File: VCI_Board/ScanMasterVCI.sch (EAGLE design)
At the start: 43 parts, among them IC1 XMEGA16A4A, IC4 SN74AHCT1G04, IC5 SN74AHCT1G04, Q5 PZT3904, Q6 MMBT3904, Q7 MMBT4403, Q8 MMBT3904/SOT, U1 MAX13444EASA+, U2 LM339MA

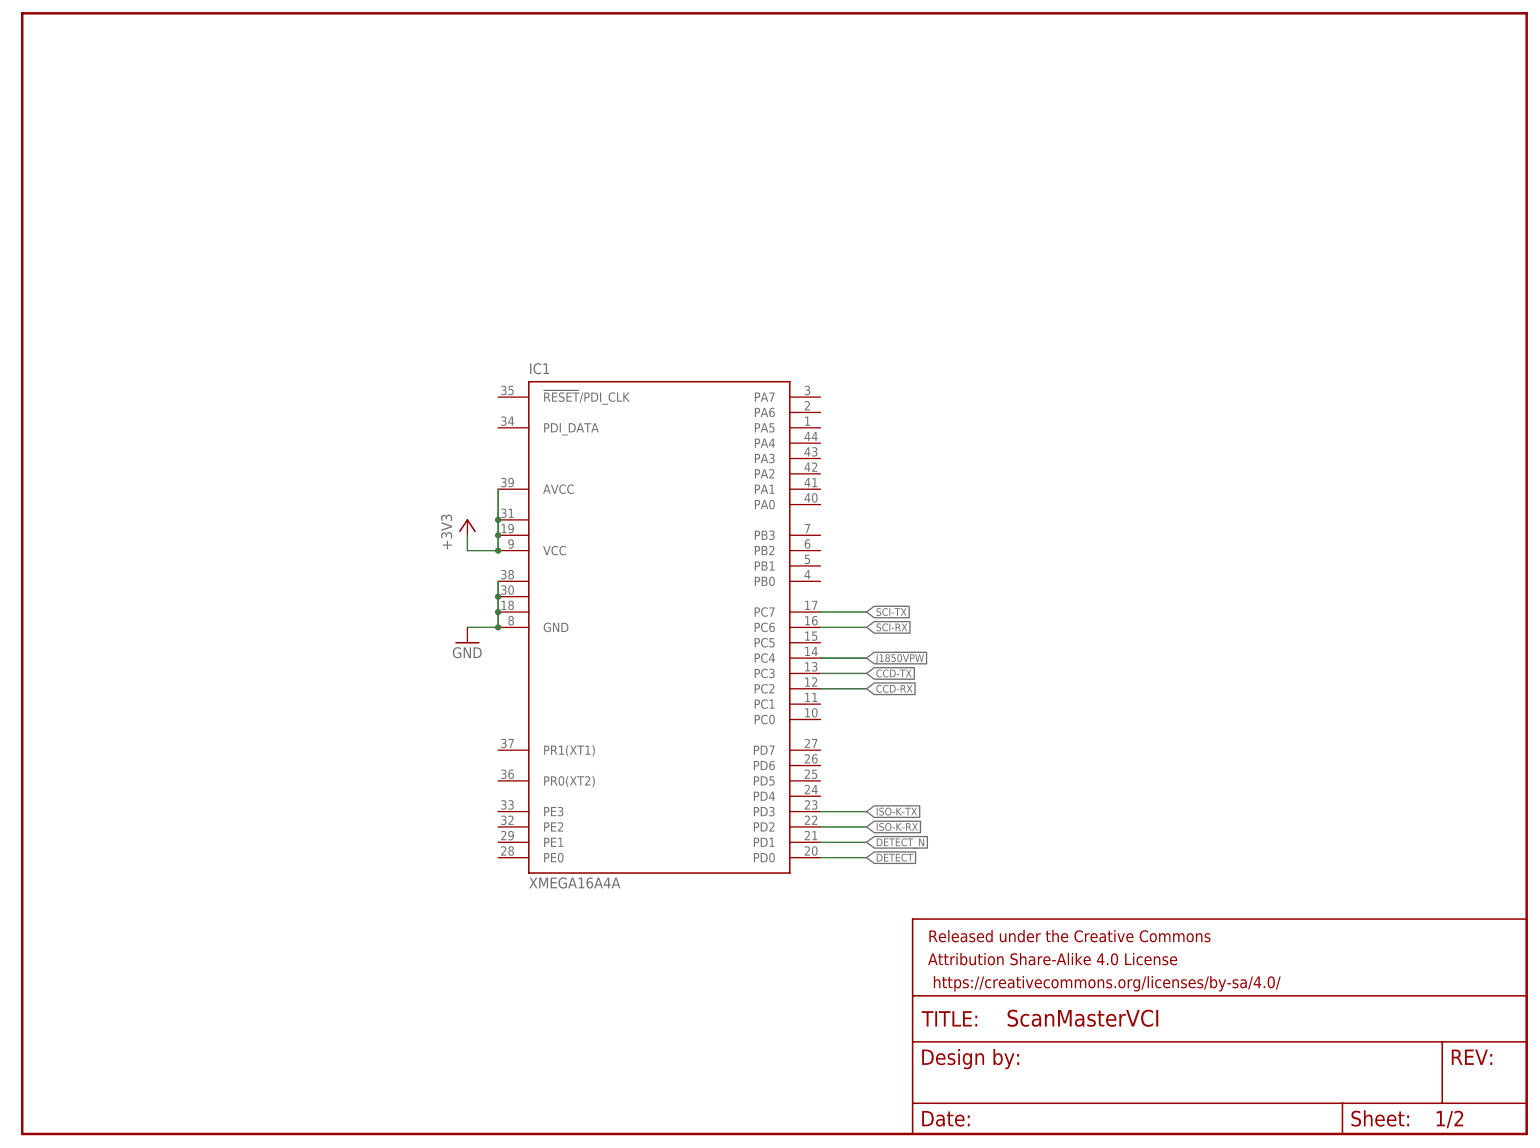
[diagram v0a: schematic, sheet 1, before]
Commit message: Begun redesigning CCD circuit. I originally based it off a J1708 circuit I found but realized that would not work.
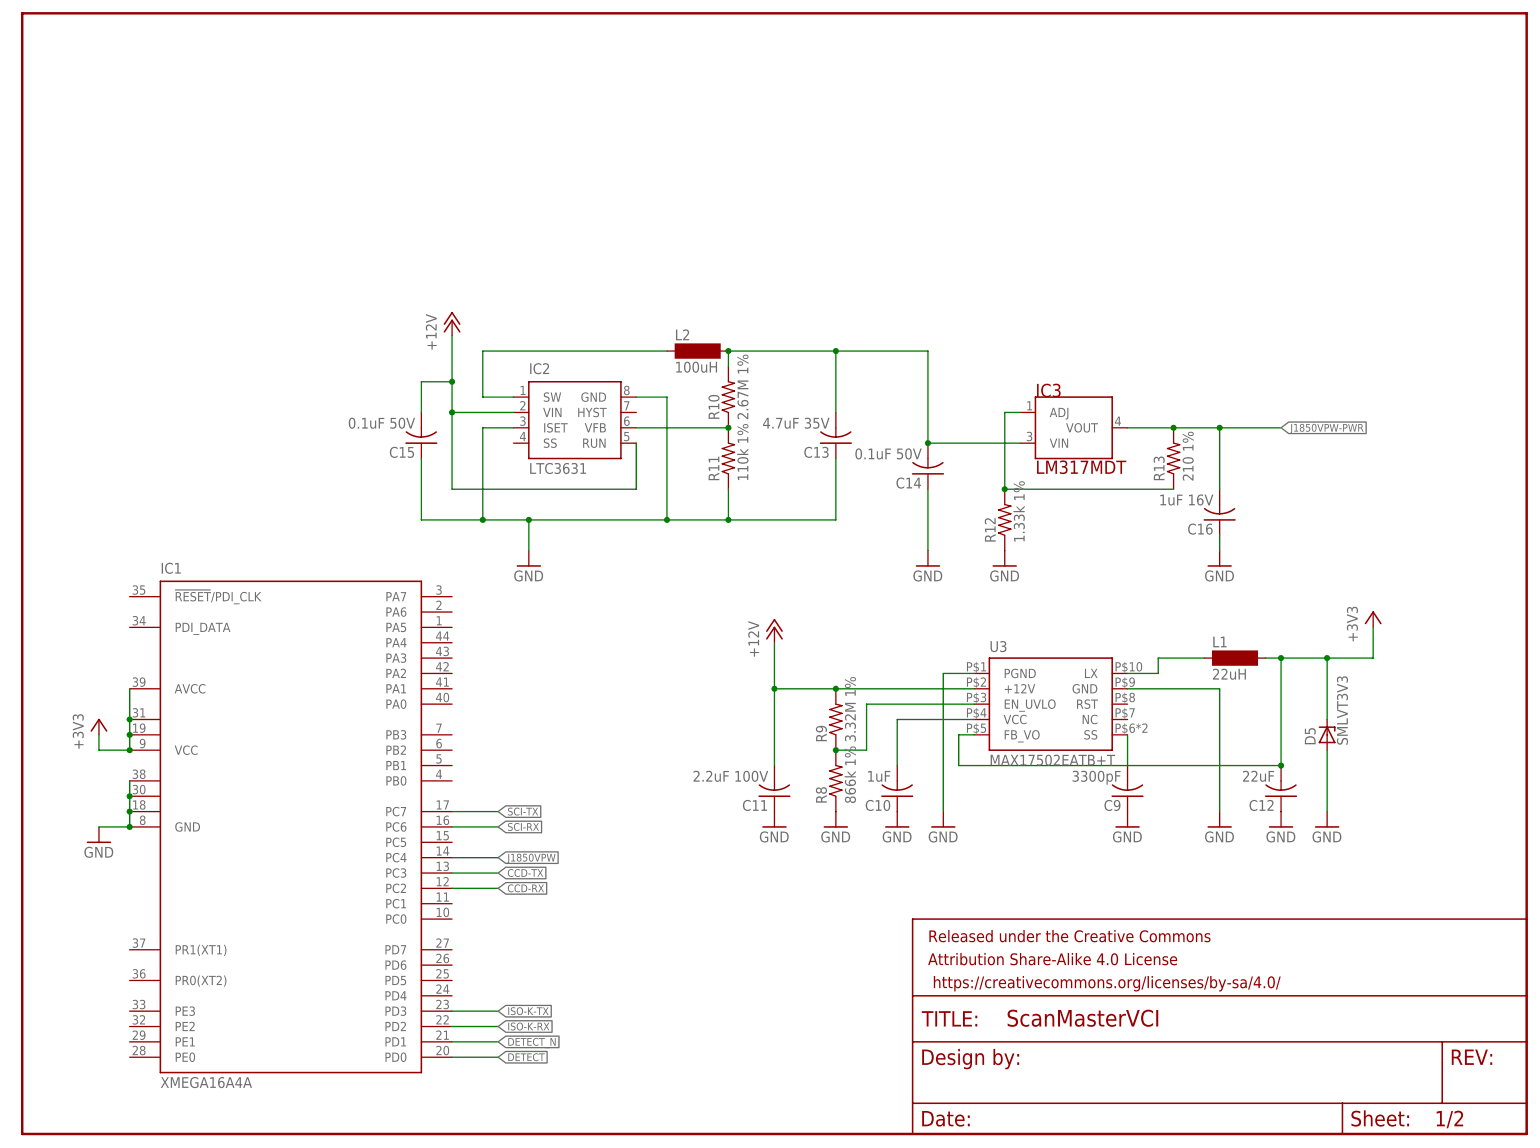
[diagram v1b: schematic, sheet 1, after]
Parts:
- removed C2: 2200pF, adafruit:C-USC0805
- removed C3: 0.1uF 16V, adafruit:C-USC0805
- removed C4: 1.0uF 16V, adafruit:C-USC0805
- removed D1, D3: SMAJ30A, diode:ZENER-DIODEZD-2.5
- removed D4: 1N4148W-7-F, diode:DIODE-D-2.5
- removed R7: (no value), adafruit:R-US_R0805
- removed U1: MAX13444EASA+, customics:MAX13444EASA+SMD
- added C10: 1uF, adafruit:C-USC0805
- added C11: 2.2uF 100V, adafruit:C-USC0805
- added C12: 22uF, adafruit:C-USC0805
- added C13: 4.7uF 35V, adafruit:C-USC0805
- added C14, C15: 0.1uF 50V, adafruit:C-USC0805
- added C16: 1uF 16V, adafruit:C-USC0805
- added C9: 3300pF, adafruit:C-USC0805
- added D5: SMLVT3V3, diode:ZENER-DIODESMB
- added IC2: LTC3631, customics:LTC3631
- added IC3: LM317MDT, customics:LM317MDT
- added IC6: TL331, linear:TL331
- added L1: 22uH, inductor-neosid:MS50
- added L2: 100uH, inductor-neosid:MS50
- added R10: 2.67M 1%, adafruit:R-US_R0805
- added R11: 110k 1%, adafruit:R-US_R0805
- added R12: 1.33k 1%, adafruit:R-US_R0805
- added R13: 210 1%, adafruit:R-US_R0805
- added R8: 866k 1%, adafruit:R-US_R0805
- added R9: 3.32M 1%, adafruit:R-US_R0805
- added U3: MAX17502EATB+T, customics:MAX17502EATB+
- added U4: MAX13444EASA+, customics:MAX13444EASA+SMD
- C1: value 2200pF -> 0.1uF 50V
- R1, R2: value 47 -> 100
- R3: value 1K -> 40.2k
- R4: value 1K -> 27.4k
- R6: value (none) -> 1M
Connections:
- removed net N$5: R6.1, U1.RO
- new net CBV: C1.2, IC6.V+
- new net J1850VPW-PWR: C16.2, IC3.VOUT, R13.2
- new net N$10: IC2.VFB, R10.1, R11.2
- new net N$11: R1.2, R4.2, U4.+
- new net N$12: L1.1, U3.LX
- new net N$13: IC2.SW, L2.1
- new net N$24: IC3.ADJ, R12.2, R13.1
- new net N$6: C13.2, C14.2, IC3.VIN, L2.2, R10.2
- new net N$7: R8.2, R9.1, U3.EN_UVLO
- new net N$8: C9.2, U3.SS
- new net N$9: C10.2, U3.VCC
- net +12V: now also C11.2, C15.2, IC2.RUN, IC2.VIN, R9.2, U3.+12V
- net +3V3: now also C12.2, D5.C, L1.2, U3.FB_VO; no longer R7.2
- net +5V: no longer C3.2, C4.2, D4.A, U1.+5V
- net CCD+: now also R2.1; no longer D3.C, R1.1
- net CCD-: now also R1.1; no longer D1.C, R2.1
- net CCD-RX: no longer R6.2
- net CCD-TX: no longer R7.1, U1.DE_N
- net GND: now also C10.1, C11.1, C12.1, C13.1, C14.1, C15.1, C16.1, C9.1, D5.A, IC2.GND, IC2.ISET, IC6.GND, R11.1, R12.1, R6.1, R8.1, U3.GND, U3.PGND; no longer C2.1, C3.1, C4.1, D1.A, D3.A, R3.1, U1.DI, U1.GND, U1.RE_N
- net N$1: now also IC6.+IN; no longer C2.2, R1.2, U1.+
- net N$2: now also IC6.-IN, R3.1, R6.2; no longer C1.2, R2.2, R3.2, U1.-
- net N$4: now also R2.2, R3.2, U4.-; no longer D4.C, R4.2
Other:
- moved on the sheet: C1, IC1, R1, R2, R3, R4, R6

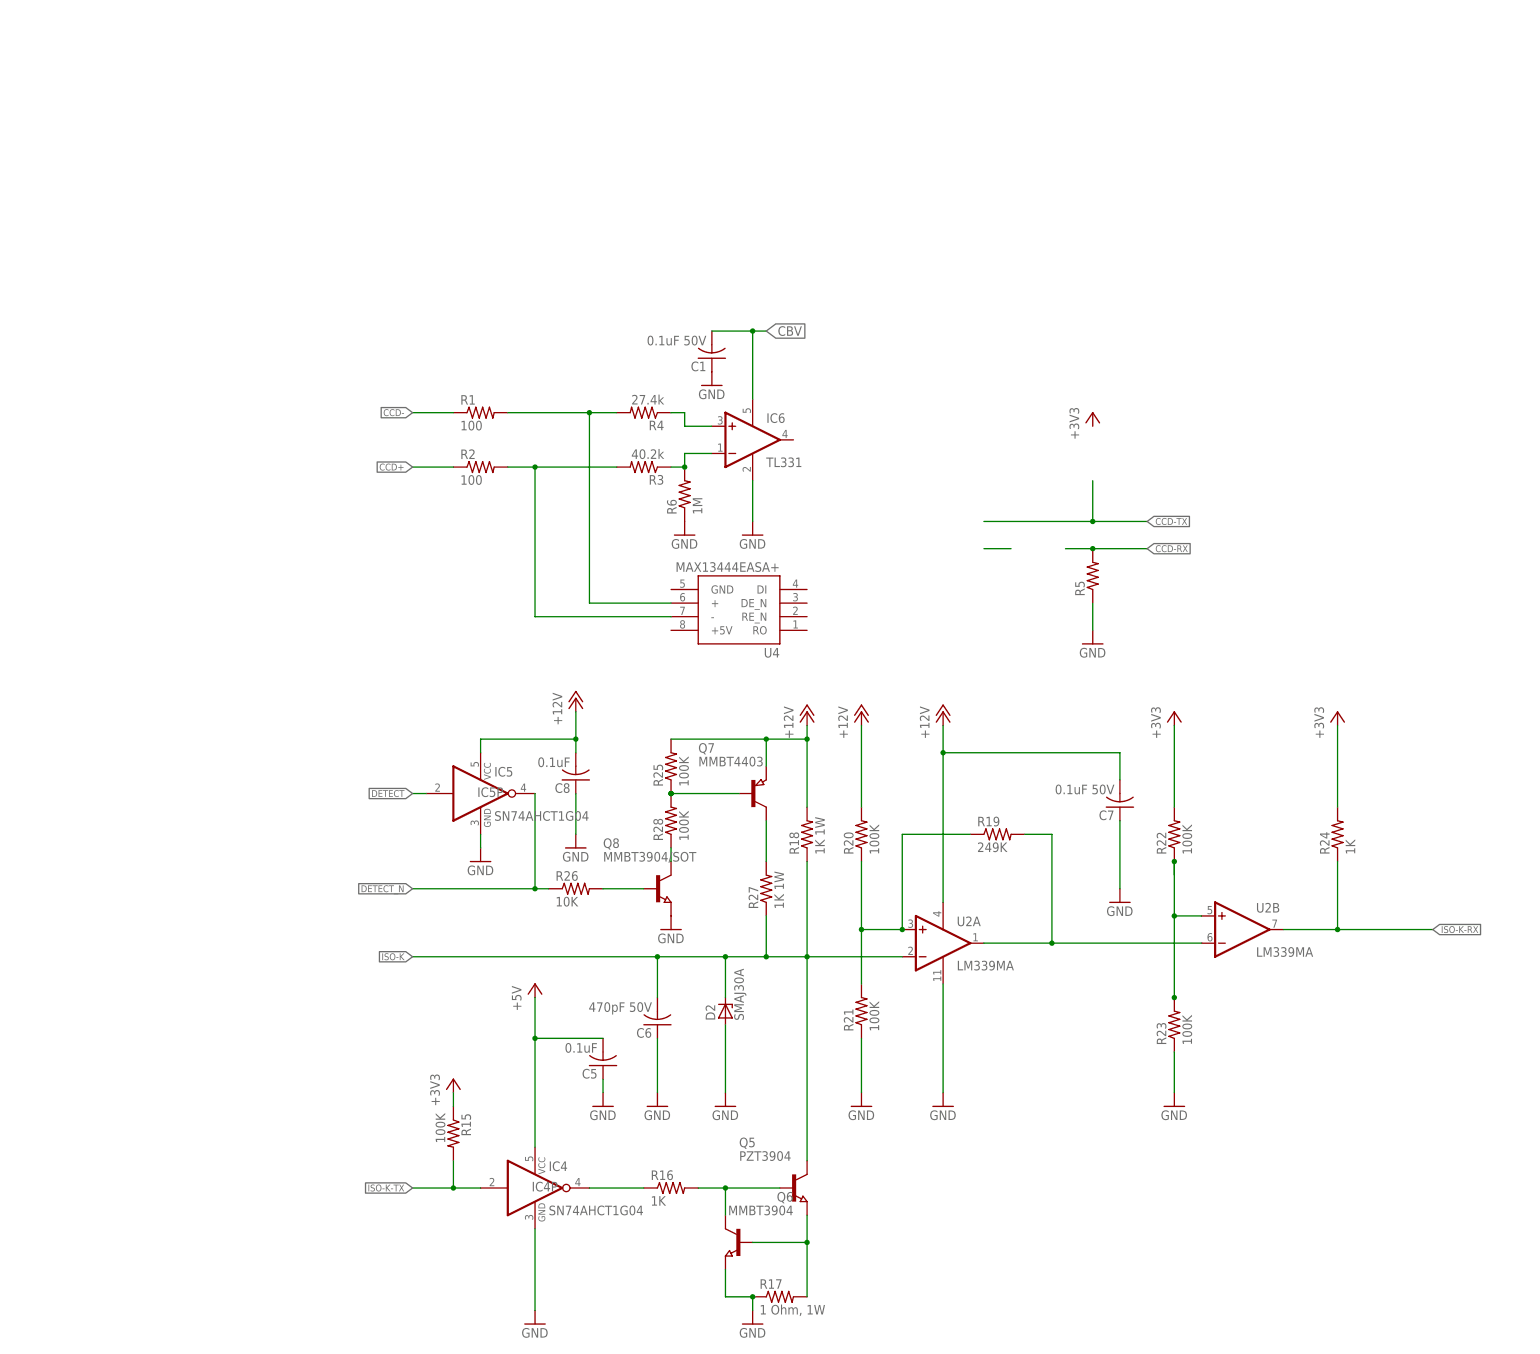
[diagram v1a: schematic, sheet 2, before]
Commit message: Finished re-working CCD. RX line should not be based off the RS485 input, so collision detection can be implemented
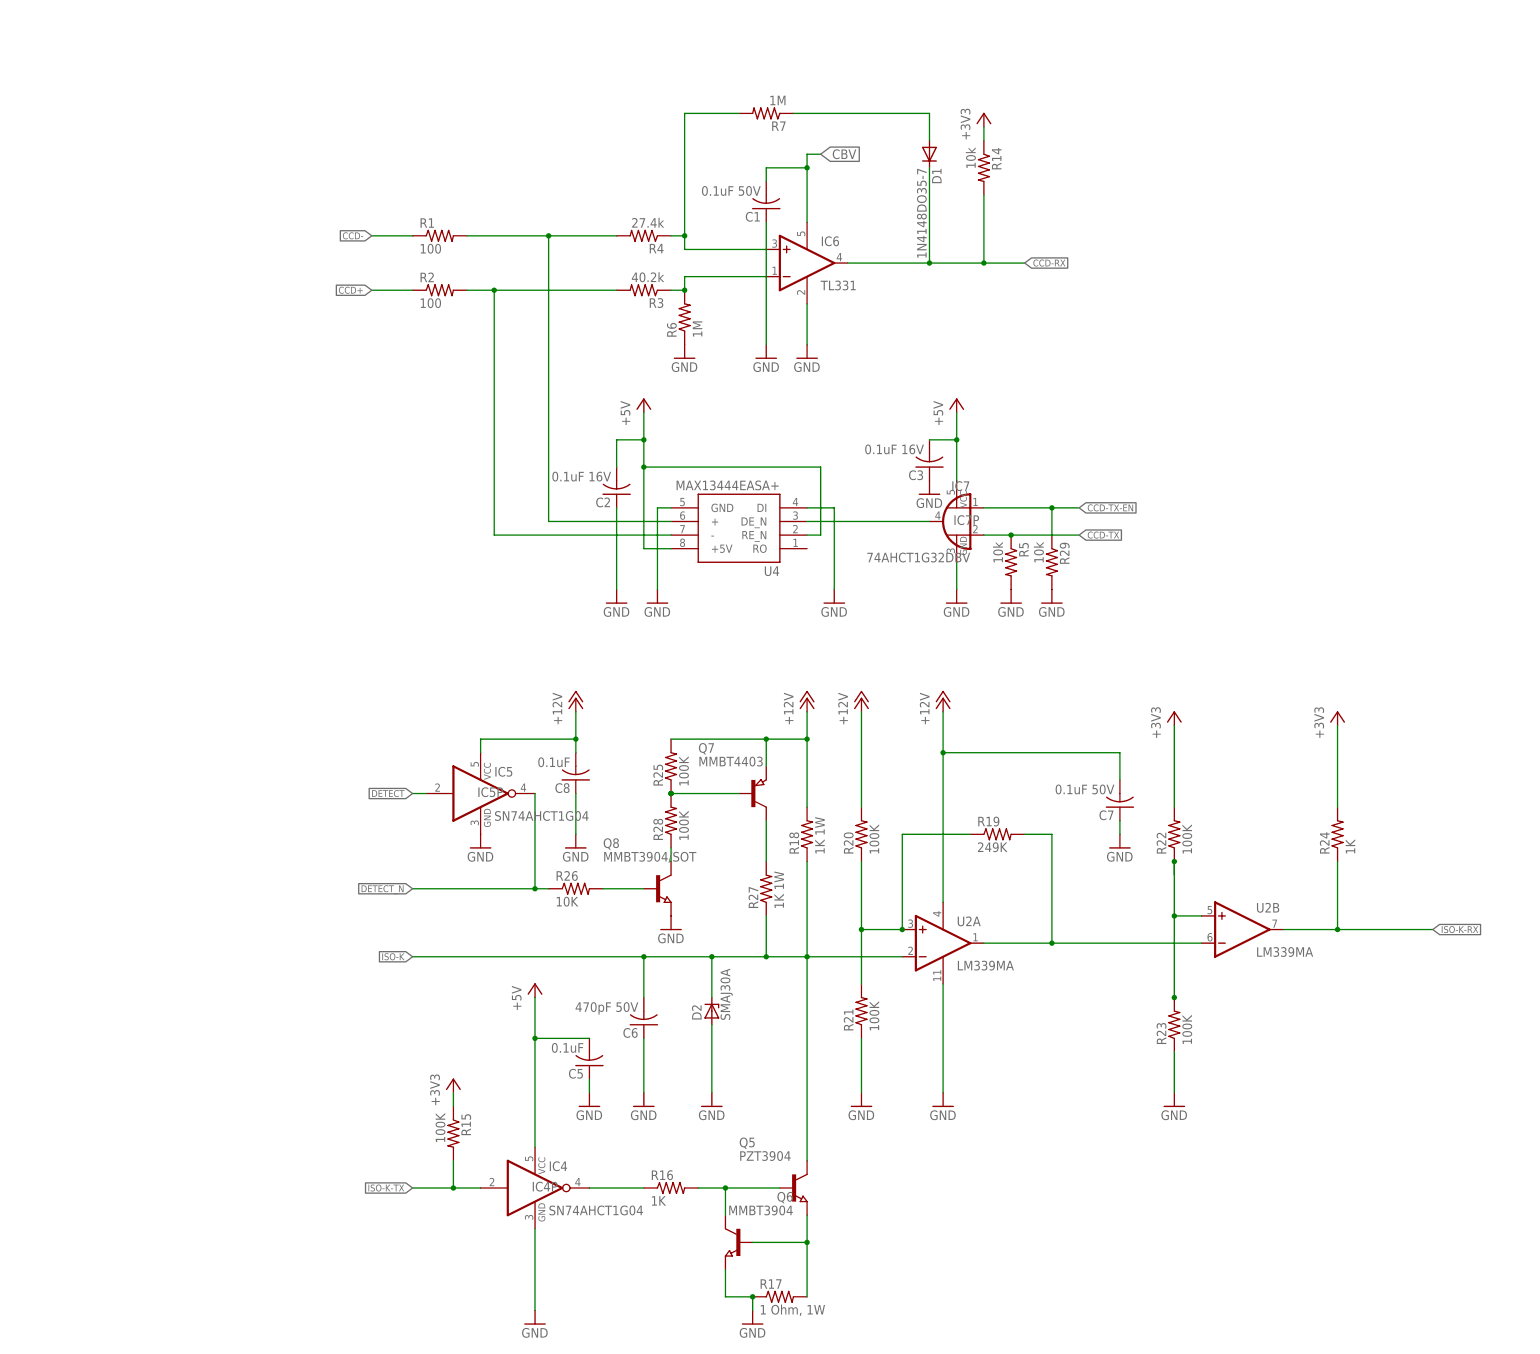
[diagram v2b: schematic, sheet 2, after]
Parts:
- added C2, C3: 0.1uF 16V, adafruit:C-USC0805
- added D1: 1N4148DO35-7, diode:1N4148DO35-7
- added IC7: 74AHCT1G32DBV, 74xx-little-de:74AHCT1G32DBV
- added R14, R29: 10k, adafruit:R-US_R0805
- added R7: 1M, adafruit:R-US_R0805
- R5: value (none) -> 10k
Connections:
- new net CCD-TX-EN: IC7A.I0, R29.1
- new net N$3: D1.A, R7.1
- net +3V3: now also R14.1
- net +5V: now also C2.2, C3.2, IC7P.VCC, U4.+5V, U4.RE_N
- net CBV: now also C13.2, C14.2, IC3.VIN, L2.2, R10.2
- net CCD-RX: now also D1.C, IC6.OUT, R14.2; no longer R5.2
- net CCD-TX: now also IC7A.I1, R5.1
- net GND: now also C2.1, C3.1, IC7P.GND, R29.2, R5.2, U4.DI, U4.GND; no longer R5.1
- net N$1: now also R7.2
- net N$6: now also IC7A.O, U4.DE_N; no longer C13.2, C14.2, IC3.VIN, L2.2, R10.2
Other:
- moved on the sheet: C1, C5, C6, D2, IC6, R1, R2, R3, R4, R5, R6, U4
